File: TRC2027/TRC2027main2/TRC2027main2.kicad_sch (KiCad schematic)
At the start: 41 parts, among them IC1 MCP23017-E_SP, J10 Memory, J11 BNO055, J12 Temperature, pressure, and al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, J13 Conn_01x03_Pin, J14 Conn_01x04_Pin, J15 Conn_01x04_Pin, J16 Conn_01x04_Pin, J17 Conn_01x04_Pin, J18 Conn_01x04_Pin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

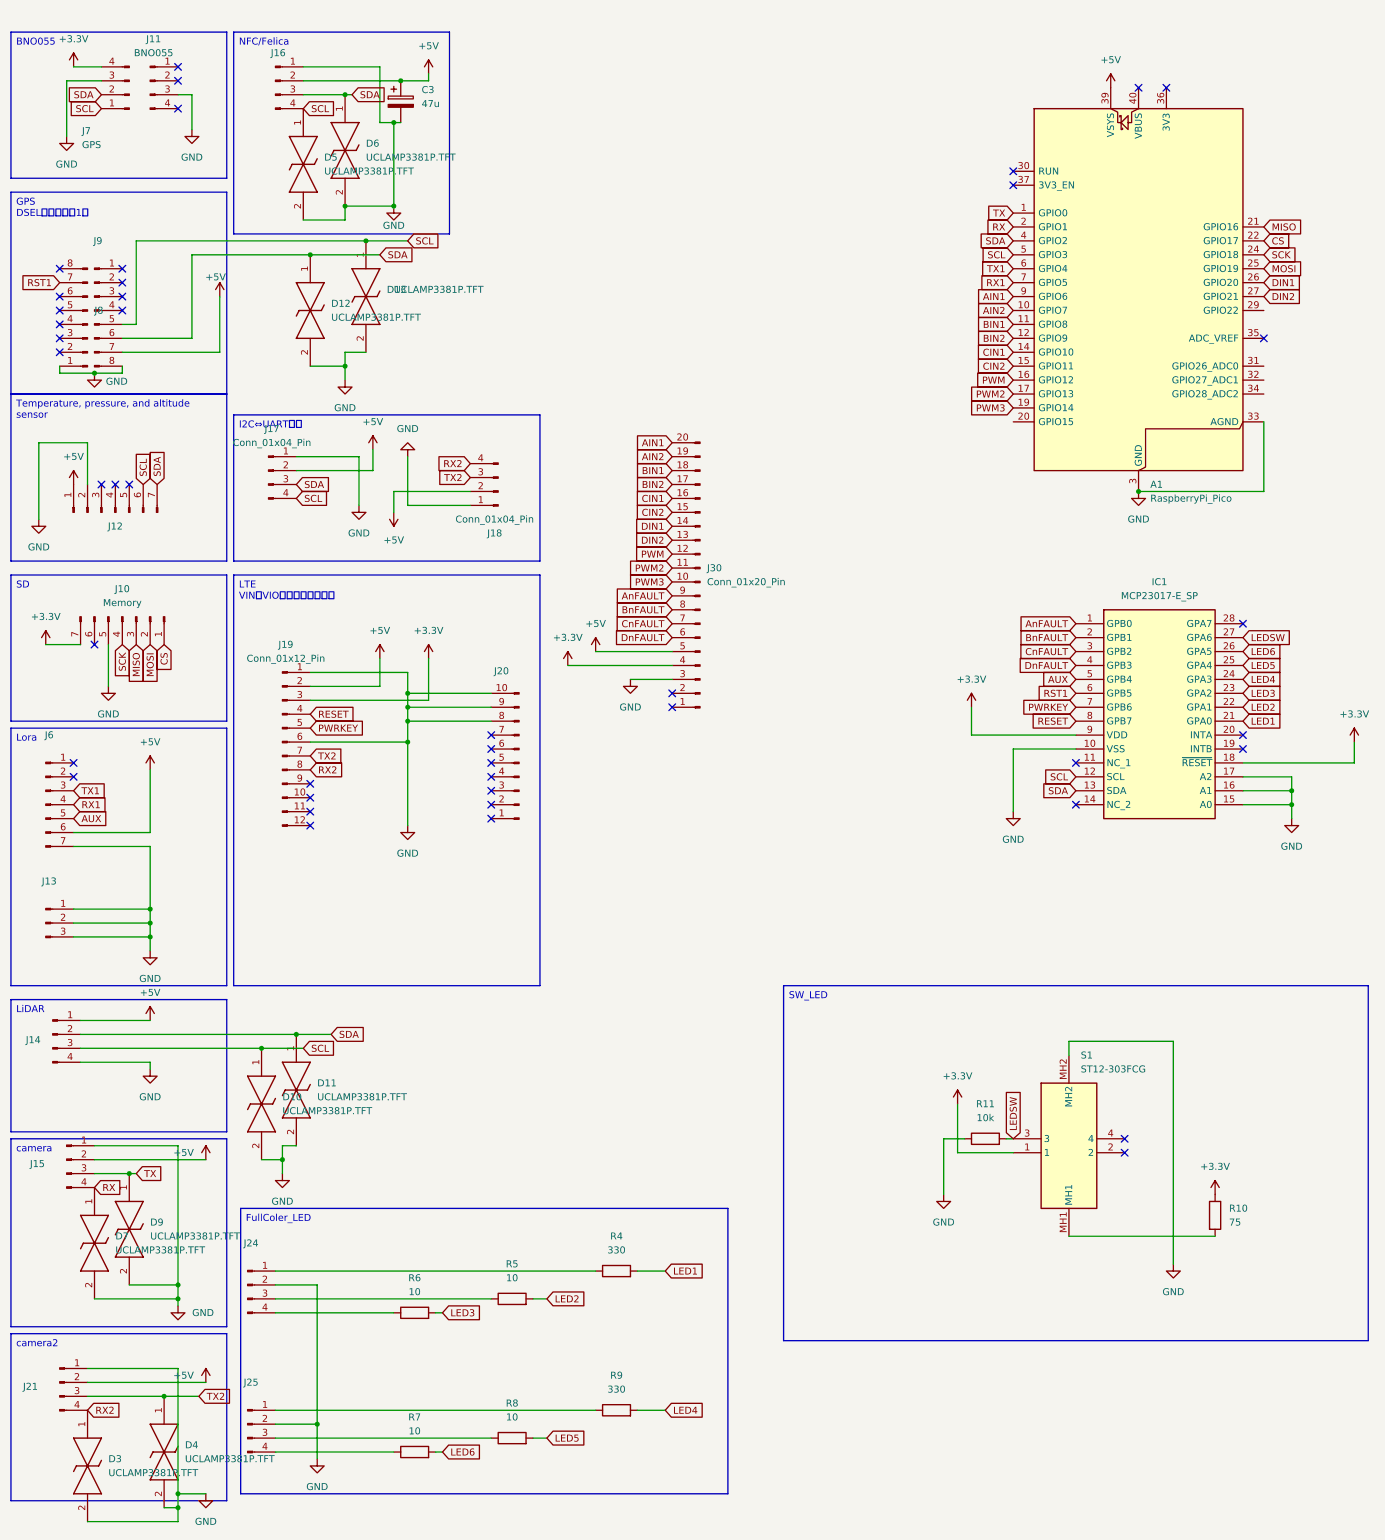
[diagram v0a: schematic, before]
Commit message: Add positions.csv file with component placements and orientations
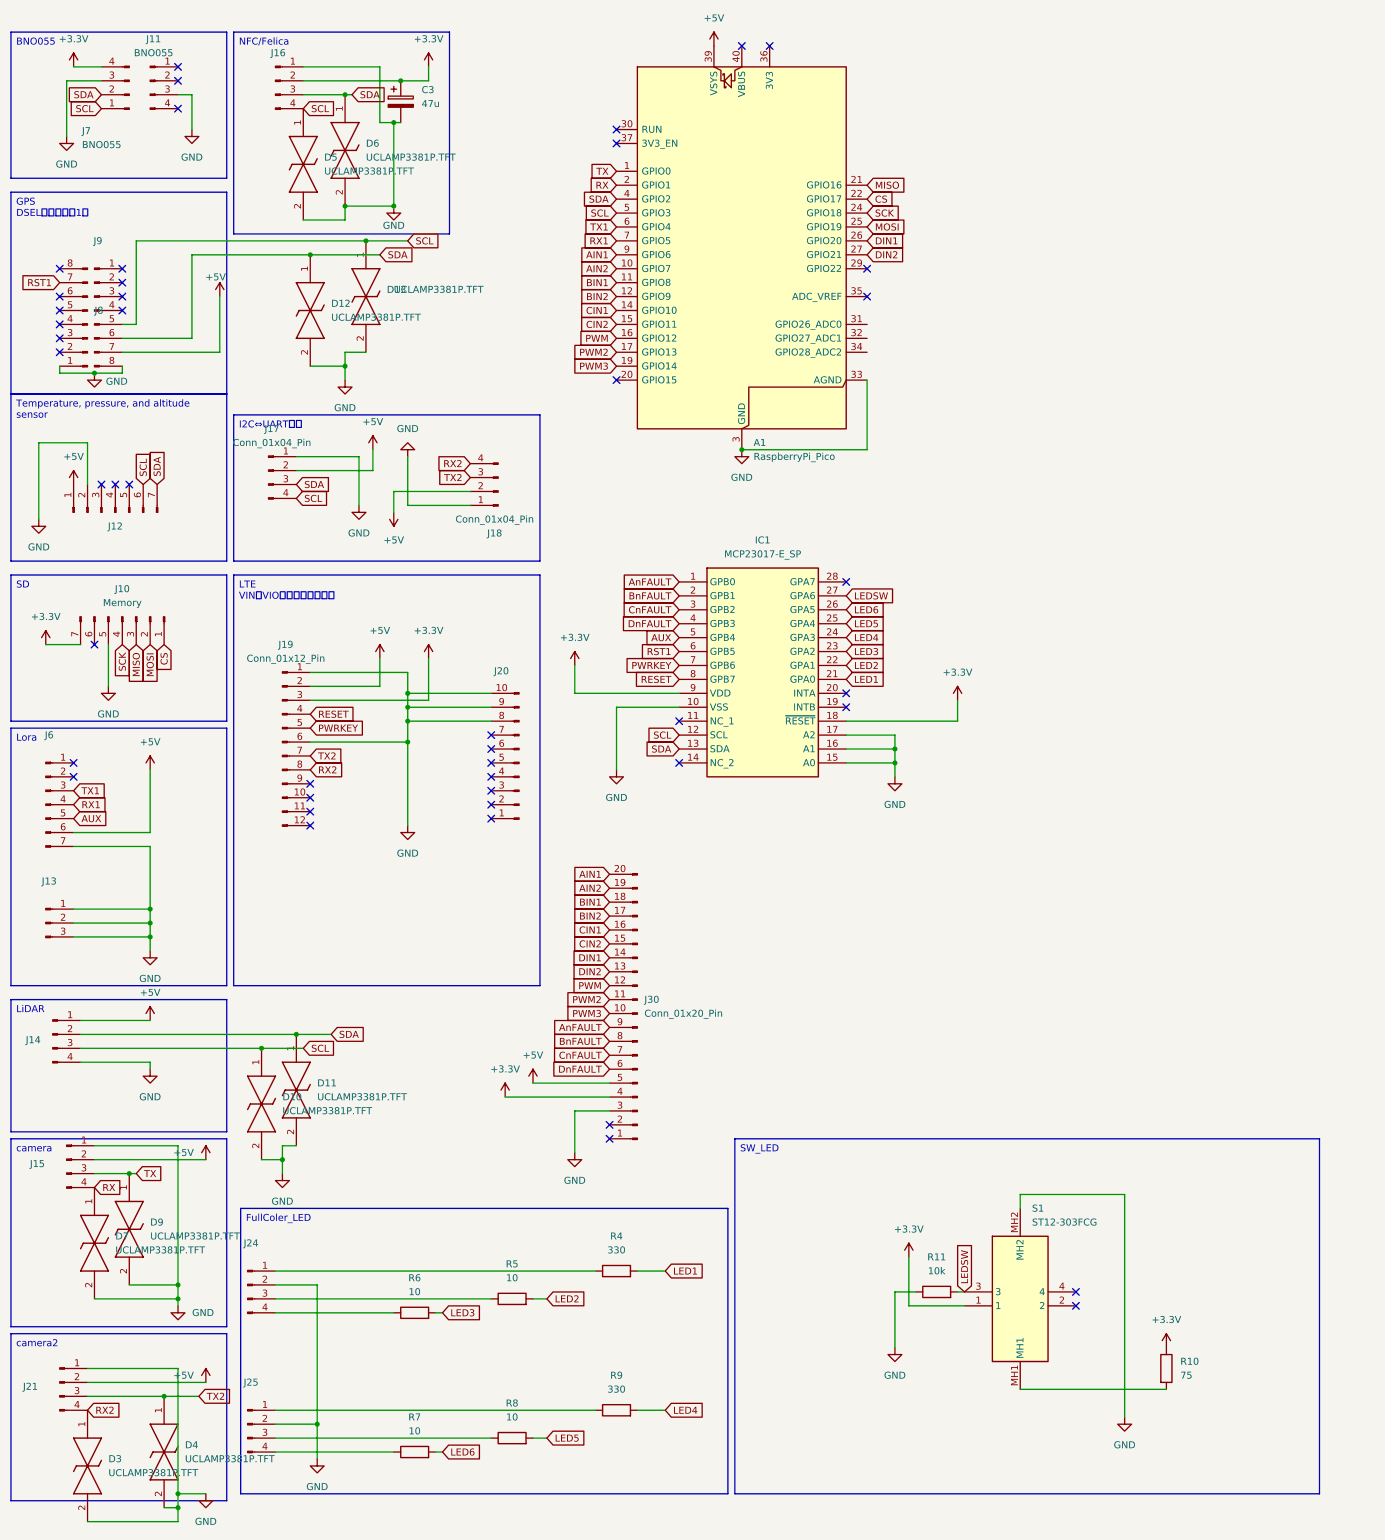
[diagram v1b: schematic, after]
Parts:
- J16: footprint Connector_PinHeader_2.54mm:PinHeader_1x04_P2.54mm_Vertical -> Connector_JST:JST_XH_B4B-XH-A_1x04_P2.50mm_Vertical
- J7: value GPS -> BNO055
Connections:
- net +3.3V: now also C3.1, J16.2 (Pin_2)
- net +5V: no longer C3.1, J16.2 (Pin_2)
- no-connect marks 44 -> 46
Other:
- moved on the sheet: A1, IC1, J30, R10, R11, S1
